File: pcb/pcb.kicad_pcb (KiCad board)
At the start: 2 copper layers, 54.6 x 86.4 mm, 2 parts, among them P8 BeagleBone_Black_Header, P9 BeagleBone_Black_Header

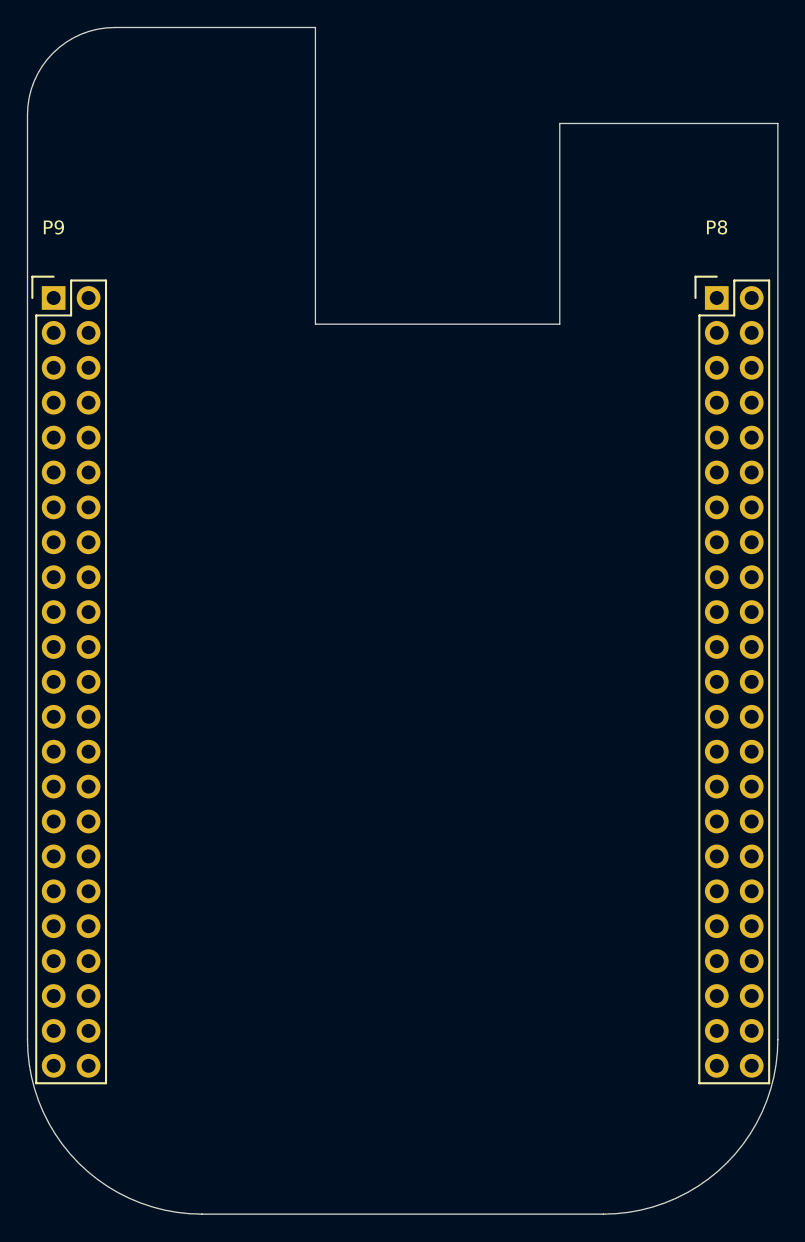
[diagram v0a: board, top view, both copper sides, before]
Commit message: Update socket to use pinheader
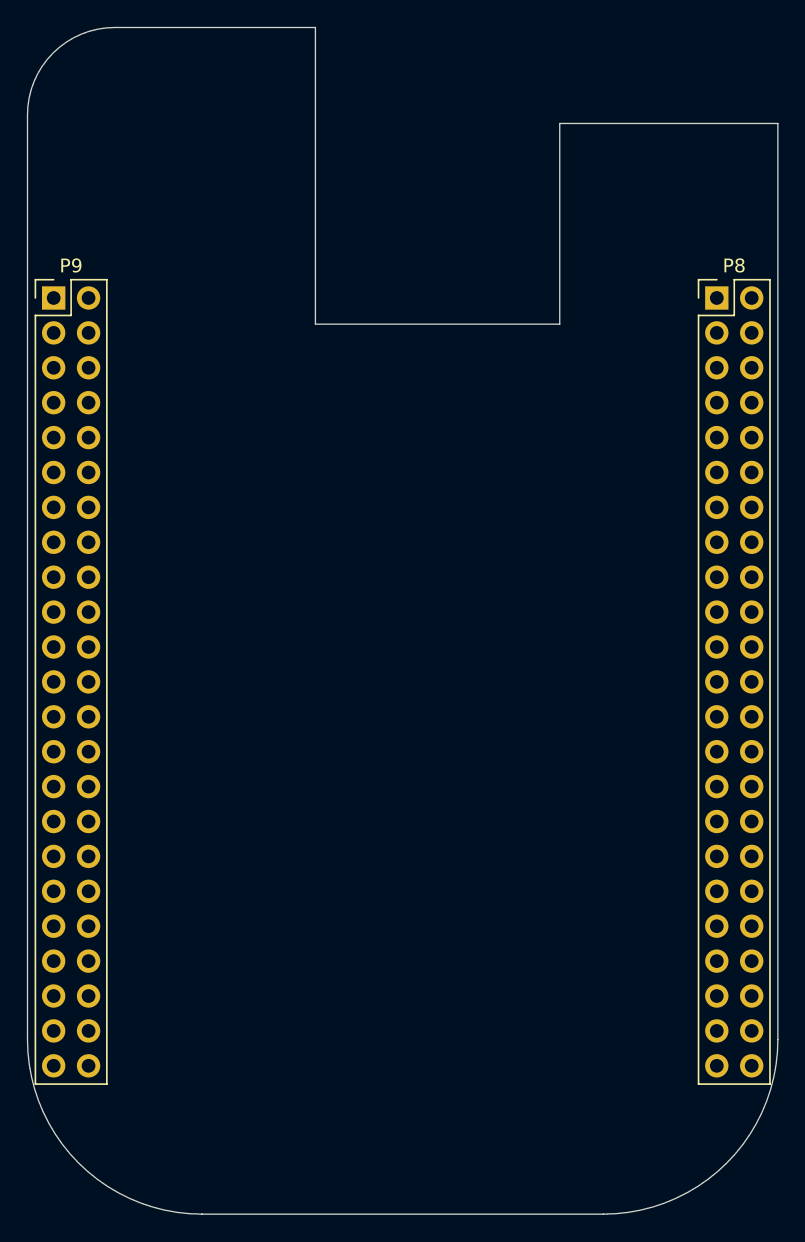
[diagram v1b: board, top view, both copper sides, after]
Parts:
- P8, P9: footprint Socket_BeagleBone_Black:Socket_BeagleBone_Black -> Connector_PinHeader_2.54mm:PinHeader_2x23_P2.54mm_Vertical
